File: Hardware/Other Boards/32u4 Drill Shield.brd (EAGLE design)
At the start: 31.8 x 55.9 mm, 16 parts, among them U1 SN74LS241DW, U2 XBEE-1B3

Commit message: Fixed a few things on shields
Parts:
- removed JP1: (no value), SparkFun-Connectors:1X03
- removed U1: SN74LS241DW, 74LS241:SOIC127P1030X265-20N
- added U$2: H_WR-TBL_321*0002VERT, MRDT-2015-PowerBoard:691321100002
- added U$4: BTM7752G, MRDT-2015-General:BTM7752G
- moved U$5 16.5 mm to (15.9, 30.0), flipped to the bottom
- moved U$3 8.57 mm to (11.1, 3.81)
- moved R1 0.95 mm to (13.3, 47.6)
- moved R11 0.95 mm to (18.4, 47.6)
- moved R3 0.95 mm to (15.9, 47.6)
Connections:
- removed net DC_1: U$1.P$16, U1.1, U1.19
- removed net DDATA_1: JP1.1, U1.2, U1.3
- removed net RX_1: U$1.P$11, U1.18
- removed net TX_1: U$1.P$12, U1.17
- new net IN1: U$4.P$9
- new net IN2: U$4.P$10
- new net INH: U$4.P$27
- new net IS: U$4.P$28
- new net OUT1: U$4.P$1, U$4.P$2, U$4.P$3, U$4.P$33, U$4.P$34, U$4.P$35, U$4.P$36, U$4.P$4
- new net OUT2: U$2.L, U$2.R, U$4.P$15, U$4.P$16, U$4.P$17, U$4.P$18, U$4.P$19, U$4.P$20, U$4.P$21, U$4.P$22
- net 12V: now also U$4.P$11, U$4.P$12, U$4.P$13, U$4.P$14, U$4.P$29, U$4.P$30, U$4.P$31, U$4.P$32; no longer JP1.2
- net 3.3V: no longer U1.20
- net GND: now also U$4.P$23, U$4.P$24, U$4.P$25, U$4.P$26, U$4.P$5, U$4.P$6, U$4.P$7, U$4.P$8; no longer JP1.3, U1.10
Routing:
- net DDATA_1: track 40.0 -> 0.00 mm
- net DC_1: track 18.2 -> 0.00 mm, vias 1 -> 0
- net 12V: track 16.0 -> 0.40 mm
- net RX_1: track 11.4 -> 0.00 mm, vias 1 -> 0
- net TX_1: track 4.28 -> 0.00 mm, vias 1 -> 0
- net RX_0: track 41.8 -> 38.4 mm
- net GND: track 3.47 -> 5.29 mm, vias 5 -> 14
- net N$4: track 2.21 -> 3.16 mm
- net N$38: track 2.21 -> 3.16 mm
- net N$1: track 2.21 -> 3.16 mm
- net TX_0: track 45.3 -> 44.8 mm, vias 2 -> 3
- added copper zone on layer 1, net 12V
- added copper zone on layer 1, net OUT1
- added copper zone on layer 1, net OUT2

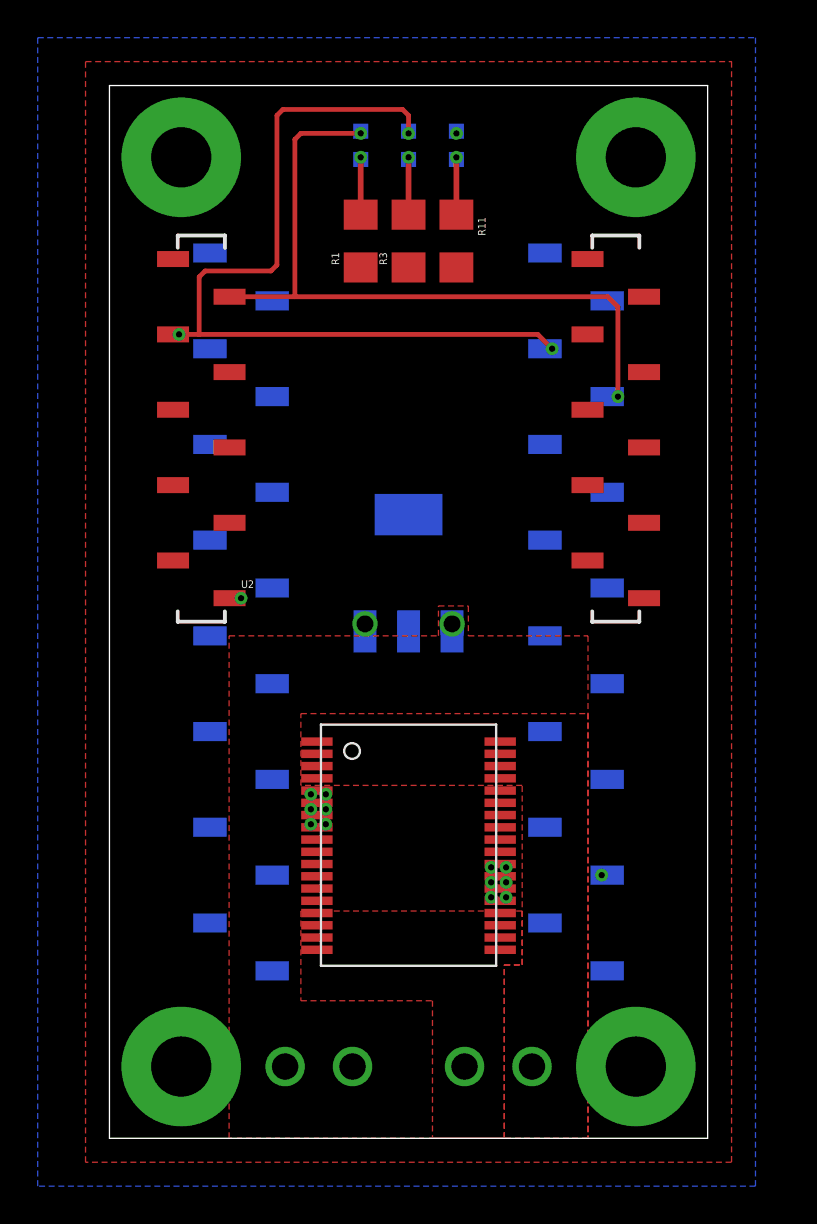
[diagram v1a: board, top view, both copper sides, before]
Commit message: Finished shields for aux
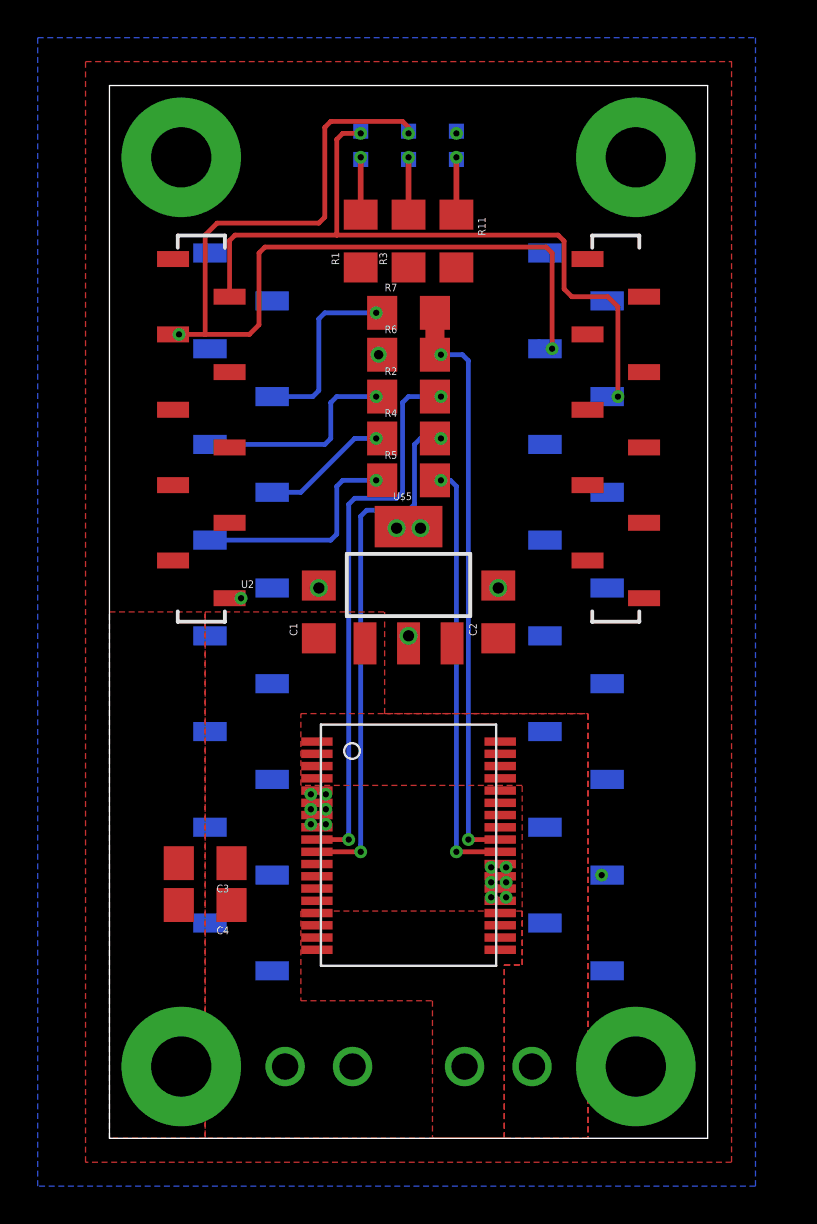
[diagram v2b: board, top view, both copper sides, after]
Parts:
- added C1, C2, C3, C4, R7: (no value), SparkFun-Passives:1206
- added R2, R4, R5: 4.7k, SparkFun-Passives:1206
- added R6: 1k, SparkFun-Passives:1206
- moved U$5 0.64 mm to (15.9, 29.4), flipped to the top
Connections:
- new net N$2: R2.2, U$4.P$9
- new net N$3: R4.2, U$4.P$10
- new net N$5: R5.2, U$4.P$27
- new net N$6: R6.2, R7.2, U$4.P$28
- net 12V: now also C1.1, C3.1, C4.1
- net 3.3V: now also C2.1
- net GND: now also C1.2, C2.2, C3.2, C4.2, R6.1
- net IN1: now also R2.1, U$1.P$28; no longer U$4.P$9
- net IN2: now also R4.1, U$1.P$27; no longer U$4.P$10
- net INH: now also R5.1, U$1.P$26; no longer U$4.P$27
- net IS: now also R7.1, U$1.P$29; no longer U$4.P$28
- net OUT1: now also U$2.R
- net OUT2: no longer U$2.R
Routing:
- net N$6: track 0.00 -> 31.7 mm, vias 0 -> 2
- net N$2: track 0.00 -> 30.1 mm, vias 0 -> 2
- net N$3: track 0.00 -> 28.5 mm, vias 0 -> 2
- net N$5: track 0.00 -> 23.4 mm, vias 0 -> 2
- net INH: track 0.00 -> 12.1 mm, vias 0 -> 1
- net IN1: track 0.00 -> 11.4 mm, vias 0 -> 1
- net IS: track 0.00 -> 10.4 mm, vias 0 -> 1
- net TX_0: track 44.8 -> 52.4 mm
- net IN2: track 0.00 -> 7.47 mm, vias 0 -> 1
- net GND: track 5.29 -> 7.61 mm, vias 14 -> 20
- net 3.3V: track 0.69 -> 0.29 mm, vias 2 -> 1
- net 12V: track 0.40 -> 0.00 mm, vias 1 -> 0
- added copper zone on layer 1, net GND
